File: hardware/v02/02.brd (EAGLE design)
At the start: 92.4 x 36.8 mm, 27 parts, among them IC2 78L05Z, IC3 MSP430G2553, X2 RJ45-6L-B

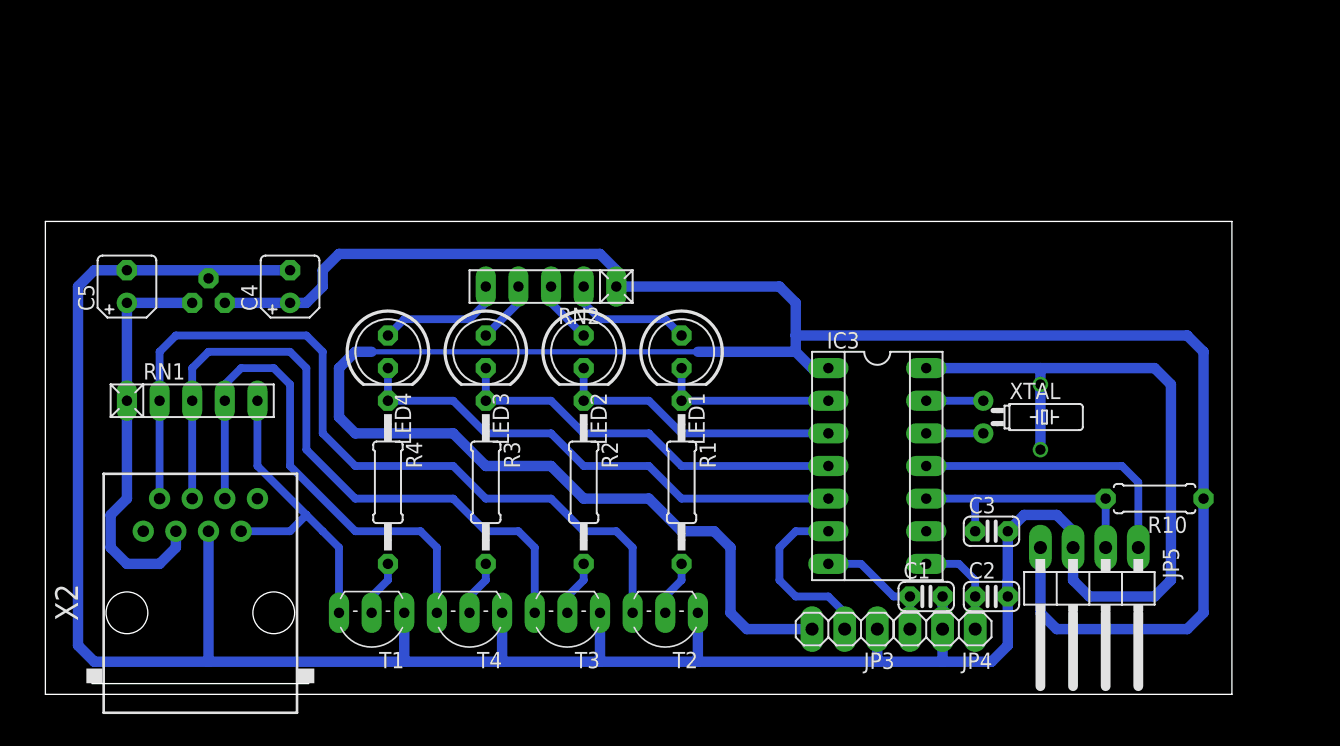
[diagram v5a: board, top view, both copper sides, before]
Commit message: denser distribution
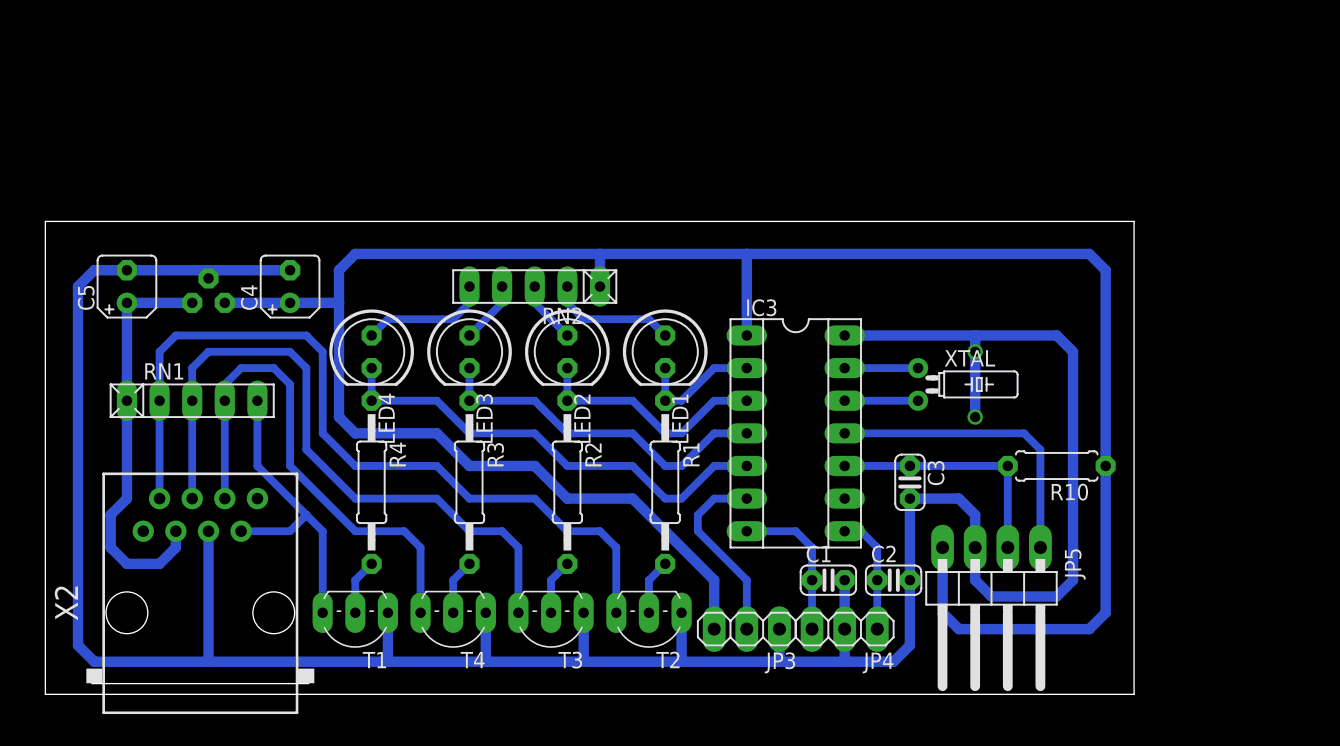
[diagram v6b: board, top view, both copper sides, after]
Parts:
- moved R10 8.03 mm to (78.7, 17.8)
- moved C1 7.73 mm to (61.0, 8.89)
- moved C2 7.73 mm to (66.0, 8.89)
- moved JP5 7.62 mm to (73.7, 7.62)
- moved JP3 7.62 mm to (54.6, 5.08)
- moved JP4 7.62 mm to (62.2, 5.08)
- moved C3 7.41 mm to (67.3, 16.5), turned to 270 degrees
- moved IC3 6.84 mm to (58.4, 20.3)
- moved XTAL 5.68 mm to (67.9, 24.1)
- moved LED1 1.27 mm to (48.3, 26.7)
- moved LED4 1.27 mm to (25.4, 26.7)
- moved R1 1.27 mm to (48.3, 16.5)
- moved R4 1.27 mm to (25.4, 16.5)
- moved T3 1.27 mm to (39.4, 5.08)
- moved T4 1.27 mm to (31.8, 5.08)
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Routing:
- net VCC: track 213.9 -> 175.0 mm
- net PR: track 31.3 -> 27.3 mm
- net N$9: track 22.6 -> 18.6 mm
- net PB: track 40.0 -> 36.0 mm
- net N$12: track 14.0 -> 9.94 mm
- net GND: track 222.0 -> 218.9 mm
- net N$3: track 9.94 -> 12.0 mm
- net OUT2: track 52.5 -> 51.2 mm
- net OUT3: track 40.5 -> 39.2 mm
- net N$6: track 22.1 -> 23.4 mm
- net OUT1: track 64.4 -> 63.2 mm
- net N$4: track 8.15 -> 9.42 mm
- net N$7: track 4.45 -> 5.71 mm
- net N$5: track 20.3 -> 19.1 mm
- net N$2: track 4.45 -> 5.71 mm
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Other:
- board size 92.4 x 36.8 mm -> 84.8 x 36.8 mm

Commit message: all caps converted to ceramic; diode over Vreg
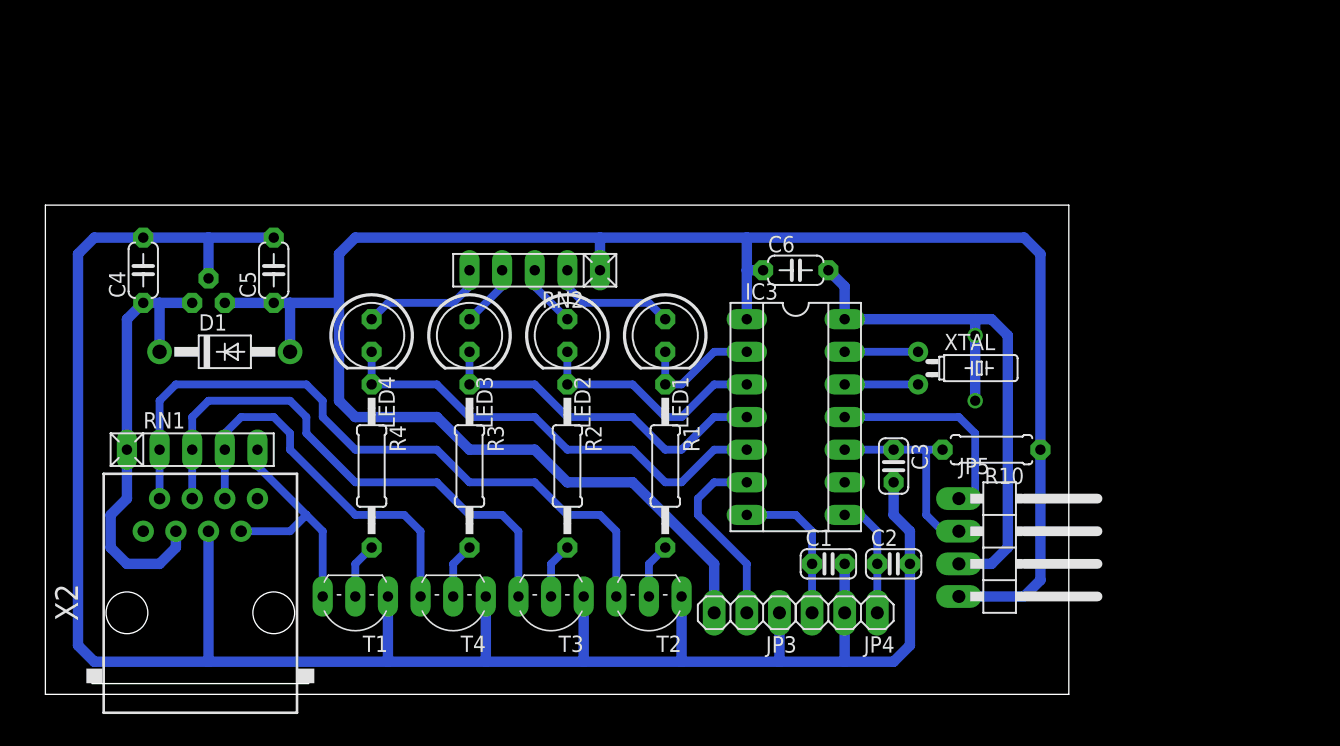
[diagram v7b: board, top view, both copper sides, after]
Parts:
- added C6: 100nF, rcl:C050-024X044
- added D1: 1N4004, adafruit:DO41-10
- C1, C2: value 100nF -> 1nF
- C4: value 200nF -> 330nF; device rcl:B45181A -> rcl:C050-024X044
- C5: value 330nF -> 100nF; device rcl:B45181A -> rcl:C050-024X044
- moved C5 11.5 mm to (17.8, 33.0)
- moved C4 11.5 mm to (7.62, 33.0)
- moved R10 5.24 mm to (73.7, 19.1)
- moved JP5 4.02 mm to (74.9, 11.4), turned to 270 degrees
- moved RN1 3.81 mm to (11.4, 19.1)
- moved C3 1.80 mm to (66.0, 17.8)
- moved RN2 1.27 mm to (38.1, 33.0)
- moved C1 1.27 mm to (61.0, 10.2)
- moved C2 1.27 mm to (66.0, 10.2)
- moved IC3 1.27 mm to (58.4, 21.6)
- moved JP3 1.27 mm to (54.6, 6.35)
- moved JP4 1.27 mm to (62.2, 6.35)
- moved LED1 1.27 mm to (48.3, 27.9)
- moved LED2 1.27 mm to (40.6, 27.9)
- moved LED3 1.27 mm to (33.0, 27.9)
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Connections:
- net +5V: now also C4.1, D1.C; no longer C5.+
- net GND: now also C4.2, C5.2, C6.2; no longer C4.-, C5.-
- net VCC: now also C5.1, C6.1, D1.A; no longer C4.+
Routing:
- net VCC: track 175.0 -> 161.8 mm
- net OUT1: track 63.2 -> 54.3 mm
- net OUT3: track 39.2 -> 30.4 mm
- net OUT2: track 51.2 -> 42.3 mm
- net N$6: track 23.4 -> 17.0 mm
- net OUT4: track 24.2 -> 19.1 mm
- net GND: track 218.9 -> 215.1 mm
- net N$5: track 19.1 -> 15.8 mm
- net +5V: track 32.1 -> 35.1 mm
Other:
- board size 84.8 x 36.8 mm -> 79.7 x 38.1 mm

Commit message: reposition XTAL
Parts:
- moved XTAL 2.54 mm to (65.4, 25.4)
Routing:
- net N$7: track 5.71 -> 3.18 mm
- net N$2: track 5.71 -> 3.18 mm
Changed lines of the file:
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@@
 <element name="C1" library="rcl" package="C025-024X044" value="1nF" x="60.96" y="10.16"/>
 <element name="C2" library="rcl" package="C025-024X044" value="1nF" x="66.04" y="10.16"/>
-<element name="XTAL" library="crystal" package="TC26H" value="" x="67.945" y="25.4" rot="R270">
-<attribute name="MF" value="" x="67.945" y="25.4" size="1.778" layer="27" rot="R270" display="off"/>
-<attribute name="MPN" value="" x="67.945" y="25.4" size="1.778" layer="27" rot="R270" display="off"/>
-<attribute name="OC_FARNELL" value="unknown" x="67.945" y="25.4" size="1.778" layer="27" rot="R270" display="off"/>
-<attribute name="OC_NEWARK" value="unknown" x="67.945" y="25.4" size="1.778" layer="27" rot="R270" display="off"/>
+<element name="XTAL" library="crystal" package="TC26H" value="" x="65.405" y="25.4" rot="R270">
+<attribute name="MF" value="" x="65.405" y="25.4" size="1.778" layer="27" rot="R270" display="off"/>
+<attribute name="MPN" value="" x="65.405" y="25.4" size="1.778" layer="27" rot="R270" display="off"/>
+<attribute name="OC_FARNELL" value="unknown" x="65.405" y="25.4" size="1.778" layer="27" rot="R270" display="off"/>
+<attribute name="OC_NEWARK" value="unknown" x="65.405" y="25.4" size="1.778" layer="27" rot="R270" display="off"/>
 </element>
 <element name="R4" library="rcl" package="0207/12" value="470" x="25.4" y="17.78" rot="R270"/>
@@
 <wire x1="3.81" y1="35.56" x2="2.54" y2="34.29" width="0.8128" layer="16"/>
 <wire x1="2.54" y1="34.29" x2="2.54" y2="3.81" width="0.8128" layer="16"/>
-<wire x1="72.39" y1="29.21" x2="73.66" y2="29.21" width="0.8128" layer="16"/>
+<wire x1="69.85" y1="29.21" x2="73.66" y2="29.21" width="0.8128" layer="16"/>
 <wire x1="73.66" y1="29.21" x2="74.93" y2="27.94" width="0.8128" layer="16"/>
 <wire x1="74.93" y1="27.94" x2="74.93" y2="11.43" width="0.8128" layer="16"/>
-<via x="72.39" y="27.94" extent="1-16" drill="0.8" shape="octagon"/>
-<wire x1="72.39" y1="27.94" x2="72.39" y2="29.21" width="0.8128" layer="16"/>
-<via x="72.39" y="22.86" extent="1-16" drill="0.8" shape="octagon"/>
-<wire x1="72.39" y1="22.86" x2="72.39" y2="27.94" width="0.8128" layer="16"/>
+<via x="69.85" y="27.94" extent="1-16" drill="0.8" shape="octagon"/>
+<wire x1="69.85" y1="27.94" x2="69.85" y2="29.21" width="0.8128" layer="16"/>
+<via x="69.85" y="22.86" extent="1-16" drill="0.8" shape="octagon"/>
+<wire x1="69.85" y1="22.86" x2="69.85" y2="27.94" width="0.8128" layer="16"/>
 <wire x1="12.7" y1="12.7" x2="12.7" y2="2.54" width="0.8128" layer="16"/>
 <contactref element="IC3" pad="14"/>
-<wire x1="62.23" y1="29.21" x2="72.39" y2="29.21" width="0.8128" layer="16"/>
+<wire x1="62.23" y1="29.21" x2="69.85" y2="29.21" width="0.8128" layer="16"/>
 <wire x1="66.04" y1="16.51" x2="66.04" y2="13.97" width="0.8128" layer="16"/>
 <wire x1="66.04" y1="13.97" x2="67.31" y2="12.7" width="0.8128" layer="16"/>
@@
 <contactref element="XTAL" pad="1"/>
 <contactref element="IC3" pad="13"/>
-<wire x1="62.23" y1="26.67" x2="67.945" y2="26.67" width="0.6096" layer="16"/>
+<wire x1="62.23" y1="26.67" x2="65.405" y2="26.67" width="0.6096" layer="16"/>
 </signal>
 <signal name="N$7">
 <contactref element="XTAL" pad="2"/>
 <contactref element="IC3" pad="12"/>
-<wire x1="62.23" y1="24.13" x2="67.945" y2="24.13" width="0.6096" layer="16"/>
+<wire x1="62.23" y1="24.13" x2="65.405" y2="24.13" width="0.6096" layer="16"/>
 </signal>
 <signal name="+5V">
